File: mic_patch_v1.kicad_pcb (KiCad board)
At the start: 4 copper layers, 40 x 31 mm, 56 parts, among them J1 Conn_ARM_SWD_TagConnect_TC203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, J2 J_000002, J3 J_000001, J4 Micro_SD_Card, J5 J_000003, SW1 SW_000001, SW2 SW_000001, U1 NORA-B106-00B, U2 PWR_nPM1100-QDXX, U3 ADAU7002ACBZ-R7, Y1 CLK_0003

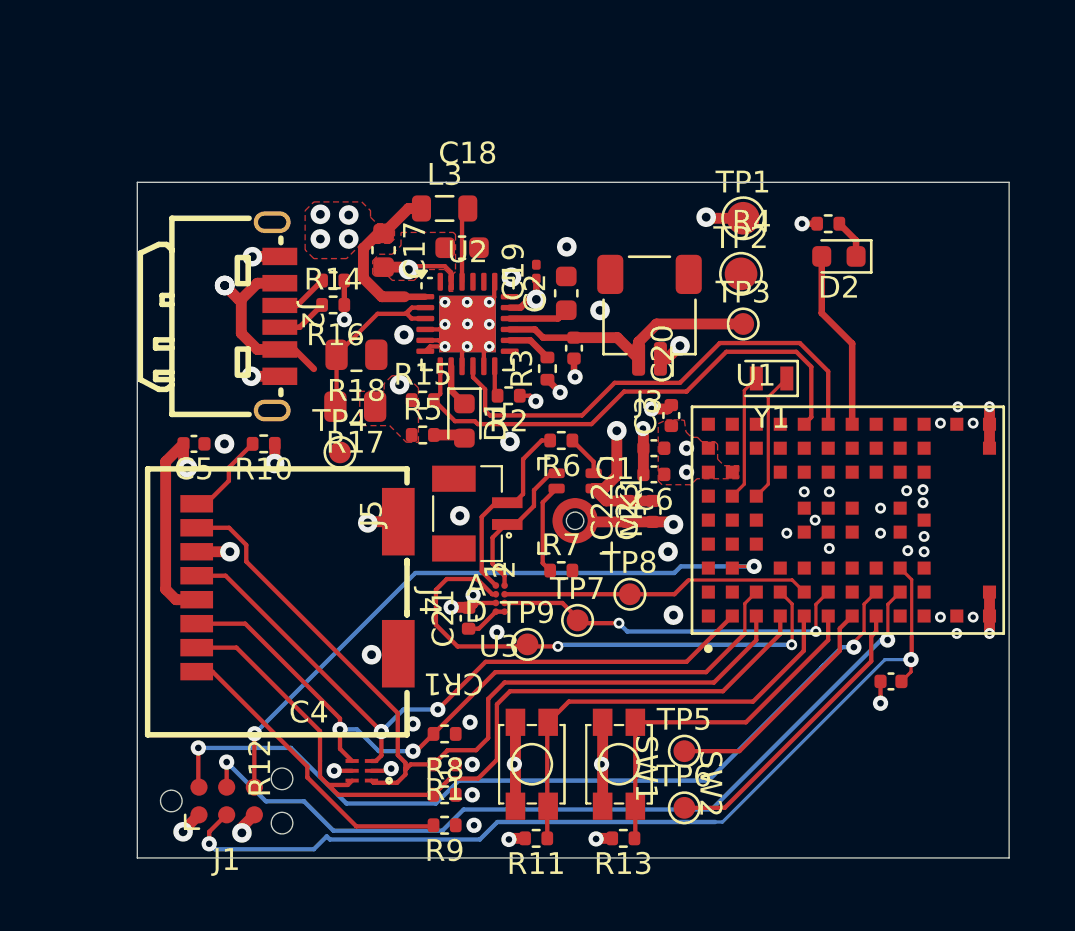
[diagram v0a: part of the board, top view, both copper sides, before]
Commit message: poured additional ground planes
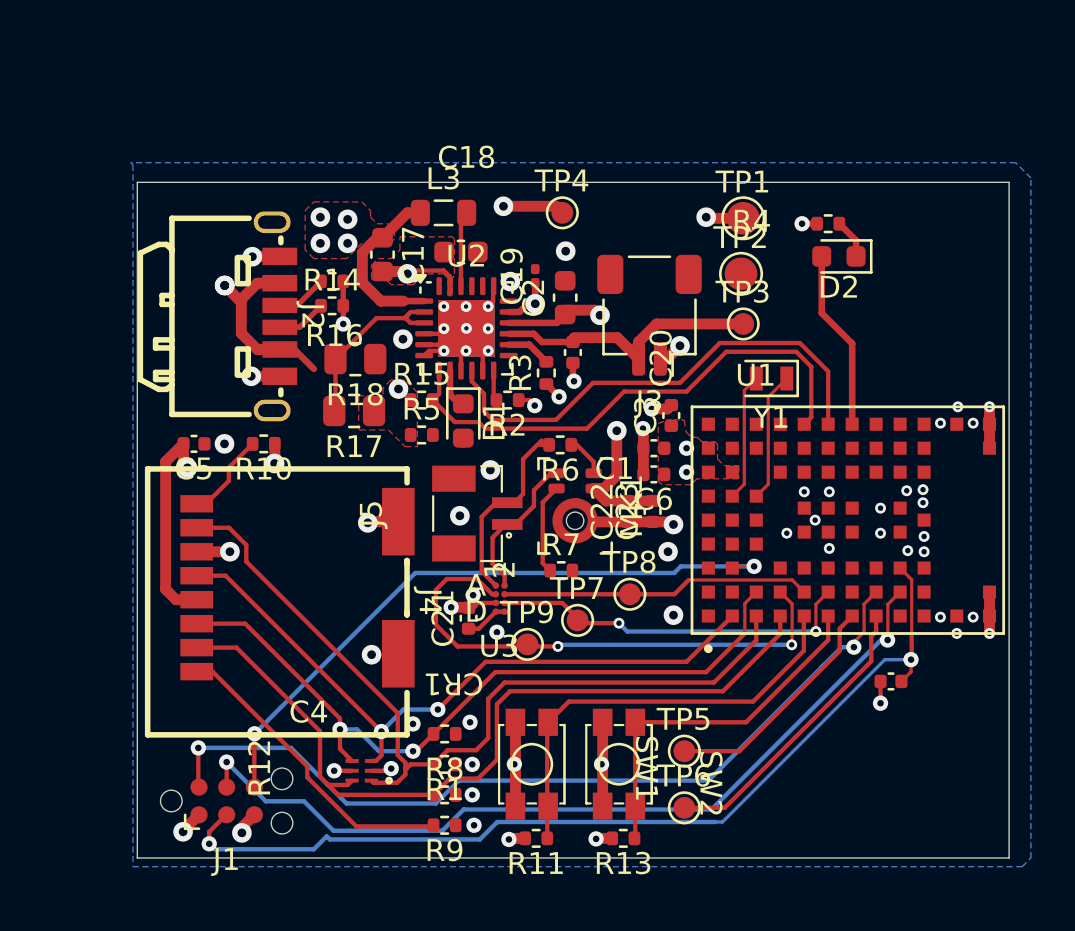
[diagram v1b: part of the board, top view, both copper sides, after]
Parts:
- moved TP4 15.0 mm to (149.4, 90.9)
- moved C18 0.21 mm to (144.8, 92.7)
- moved C19 0.21 mm to (148.2, 93.8)
- moved L3 0.21 mm to (143.9, 90.9)
- moved R17 0.21 mm to (139.8, 100.0)
- moved R3 0.21 mm to (148.7, 98.2)
- moved R6 0.21 mm to (149.3, 101.5)
- moved U2 0.21 mm to (145.0, 96.2)
- moved R2 0.21 mm to (146.9, 99.5)
- moved C2 0.21 mm to (149.5, 94.8)
- moved C20 0.21 mm to (149.9, 97.3)
- moved R18 0.21 mm to (139.9, 97.6)
- moved C17 0.21 mm to (141.2, 92.8)
- moved R16 0.06 mm to (138.8, 94.0)
- moved R14 0.06 mm to (138.8, 95.2)
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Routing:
- net +3V0 VDD_NRF: track 152.2 -> 189.1 mm
- net GND: track 49.0 -> 40.5 mm
- net /Power/VBUS: track 30.6 -> 34.8 mm, vias 3 -> 4
- net VSYS: track 13.6 -> 15.6 mm
- net Net-(D1-A): track 1.46 -> 0.21 mm
- added copper zone on In2.Cu, net +3V0 VDD_NRF
- added copper zone on B.Cu, net GND
- added copper zone on In2.Cu, net GND

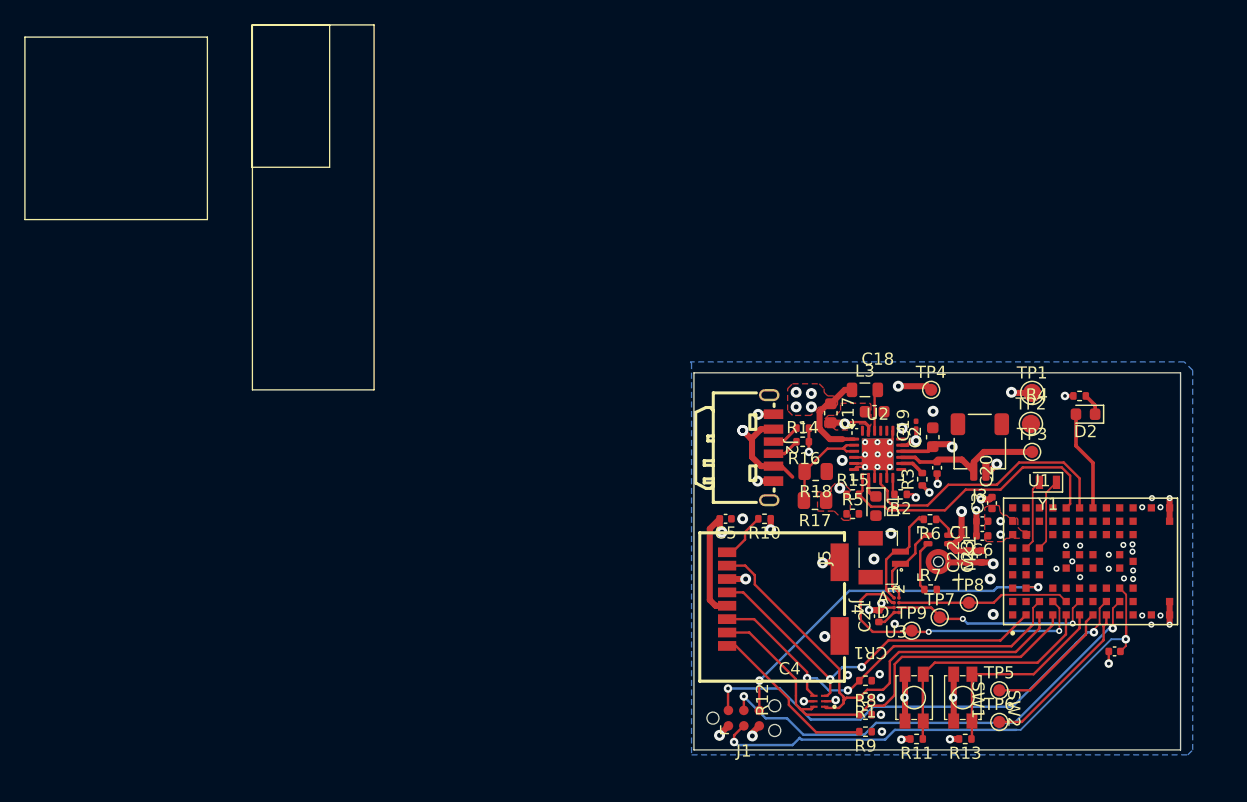
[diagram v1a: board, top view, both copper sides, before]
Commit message: fixed all major DRC warnings and errors
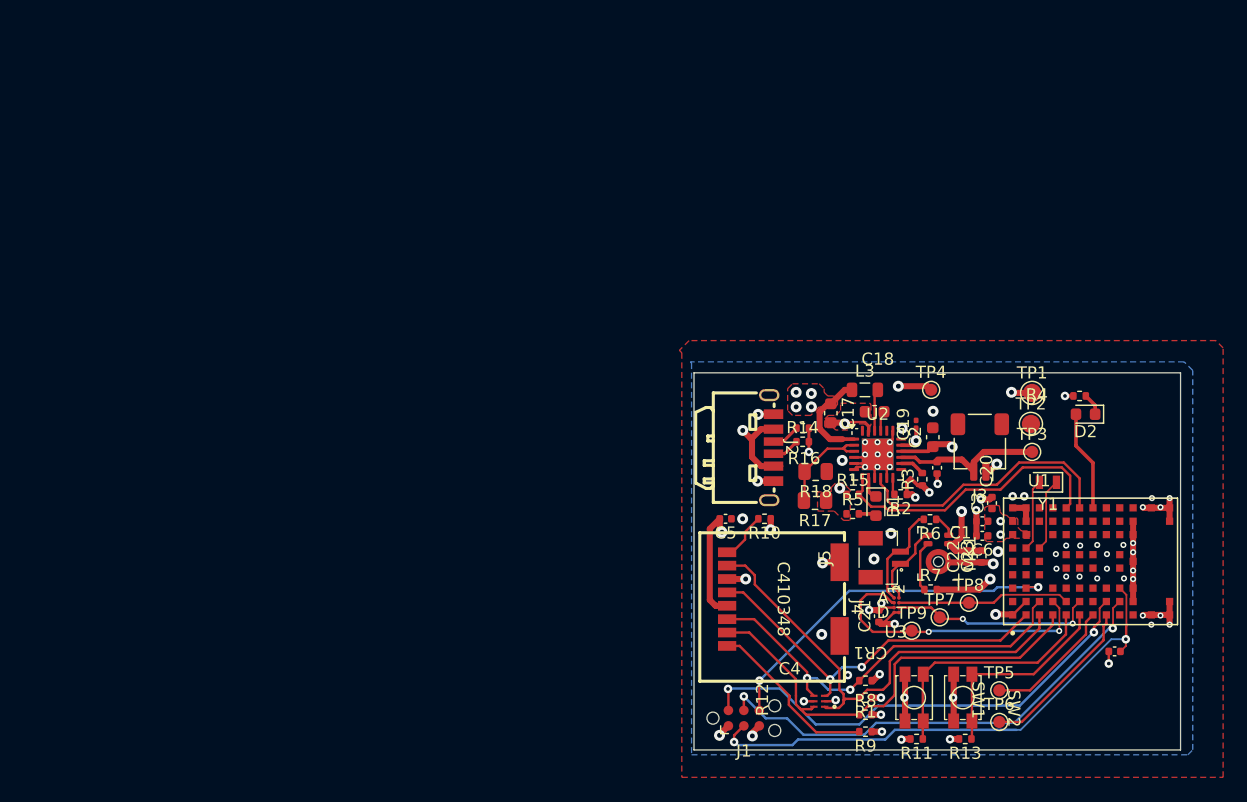
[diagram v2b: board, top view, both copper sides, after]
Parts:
- moved C19 0.07 mm to (148.2, 93.7)
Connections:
- J4 pad 10: (no net) -> GND
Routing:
- net GND: track 40.5 -> 64.1 mm, vias 62 -> 68
- net +3V0 VDD_NRF: track 189.1 -> 194.9 mm
- net /Power/DEC_NPM: track 0.00 -> 1.68 mm
- net Net-(D1-A): track 0.21 -> 1.66 mm
- net /Power/VBUS: track 34.8 -> 33.8 mm, vias 4 -> 3

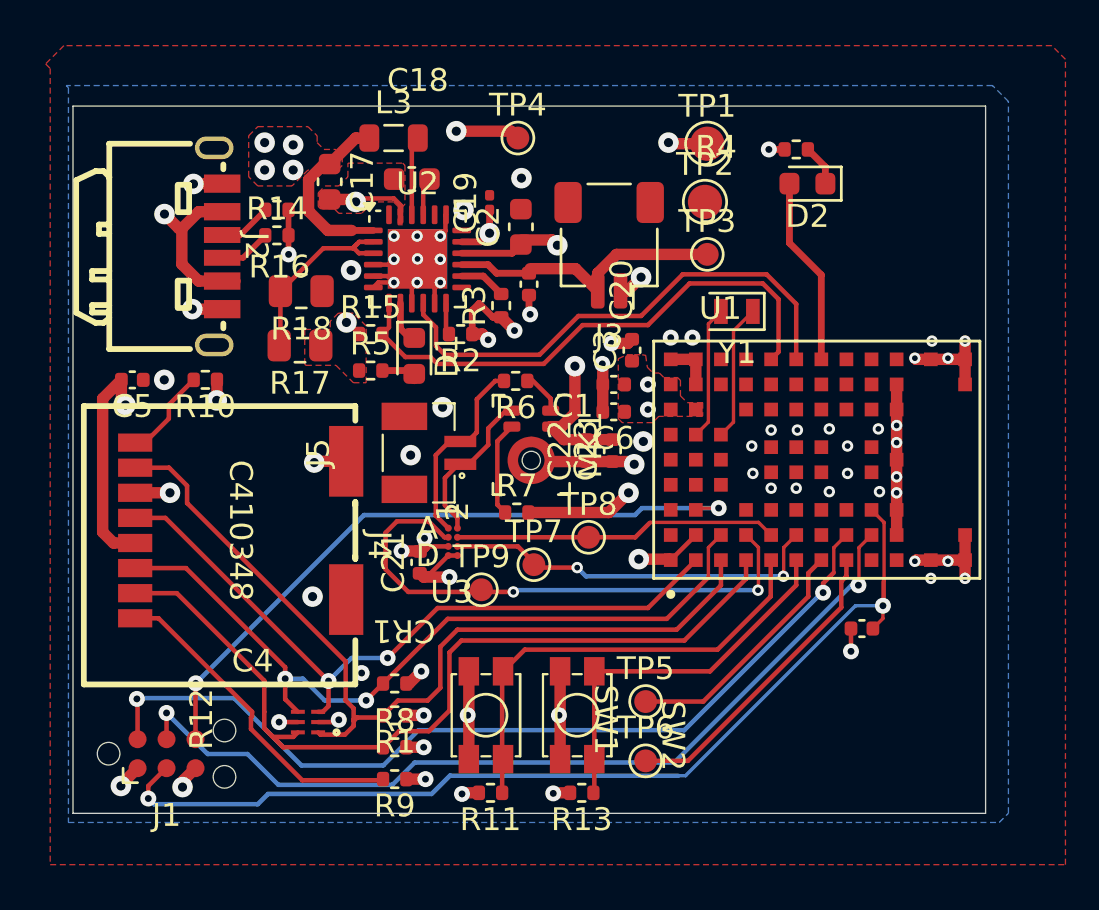
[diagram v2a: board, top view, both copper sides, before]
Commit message: added silkscreen
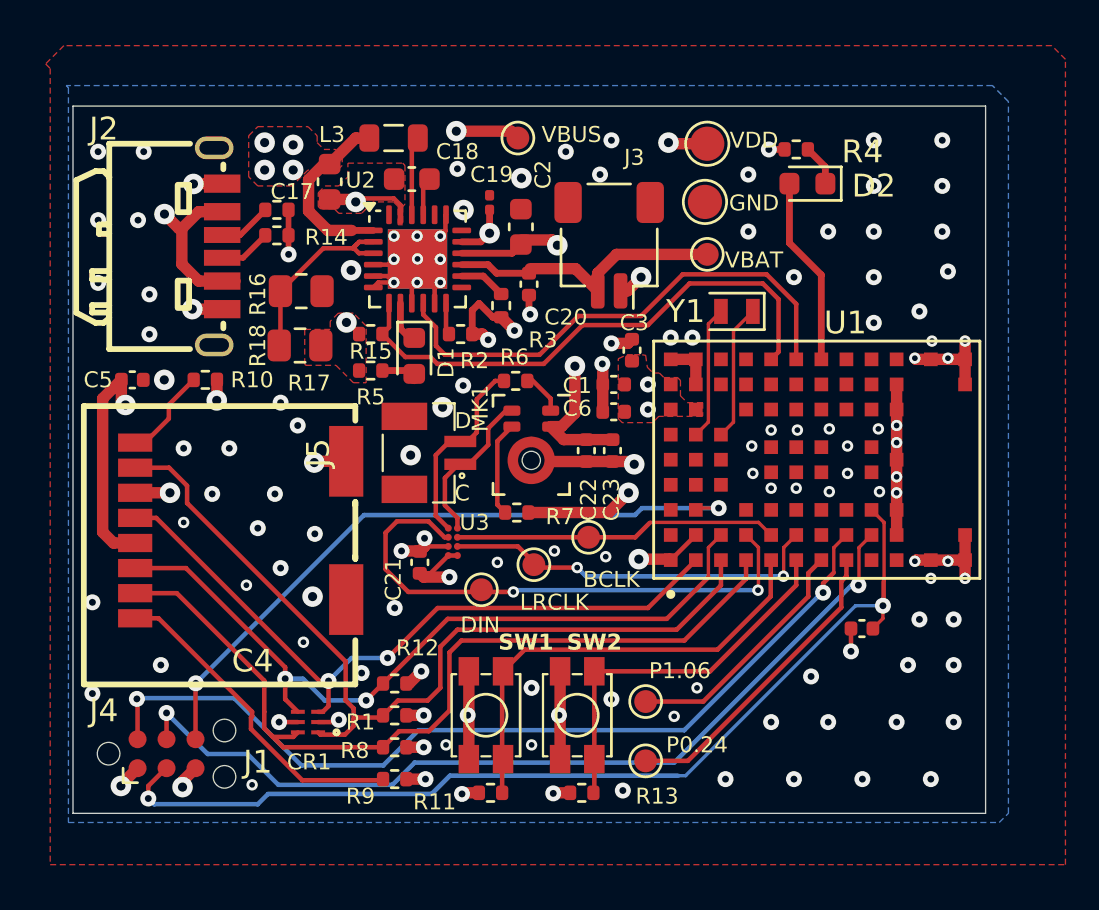
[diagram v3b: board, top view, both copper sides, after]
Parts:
- renumbered TP8 to BCLK, TP9 to DIN, TP2 to GND, TP7 to LRCLK, TP6 to P0.24, TP5 to P1.06, TP3 to VBAT, TP4 to VBUS, TP1 to VDD
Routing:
- net GND: vias 68 -> 133
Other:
- board text added: "C"
- board text added: "D"

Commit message: removed PDM series termination resistor under guidance from MS-2472 analogue devices
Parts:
- removed R6: R_00005, Resistor_SMD:R_0402_1005Metric
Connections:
- MK1 pad 1: Net-(MK1-DATA) -> /Mic/PDM_DAT
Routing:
- net Net-(MK1-DATA): track 1.91 -> 0.00 mm
- net /Mic/PDM_DAT: track 8.62 -> 10.5 mm

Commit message: final tweaks
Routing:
- net GND: vias 133 -> 134
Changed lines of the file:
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@@
 	)
 	(via
-		(at 139 102.5)
+		(at 138.75 102.25)
 		(size 0.7)
 		(drill 0.3)
@@
 		(size 0.7)
 		(drill 0.3)
+		(layers "F.Cu" "B.Cu")
+		(free yes)
+		(net 1)
+	)
+	(via
+		(at 151.5 99.75)
+		(size 0.5)
+		(drill 0.25)
 		(layers "F.Cu" "B.Cu")
 		(free yes)
@@
 	)
 	(segment
+		(start 145.809 99.199)
+		(end 145.809 100.009)
+		(width 0.2)
+		(layer "F.Cu")
+		(net 12)
+	)
+	(segment
+		(start 151.05 98.7)
+		(end 154.8 98.7)
+		(width 0.2)
+		(layer "F.Cu")
+		(net 12)
+	)
+	(segment
 		(start 145.25 98.64)
 		(end 145.809 99.199)
@@
 	)
 	(segment
+		(start 154.8 98.7)
+		(end 156.625 96.875)
+		(width 0.2)
+		(layer "F.Cu")
+		(net 12)
+	)
+	(segment
+		(start 161.6 98.175)
+		(end 161.6 100.6)
+		(width 0.2)
+		(layer "F.Cu")
+		(net 12)
+	)
+	(segment
+		(start 149.35 100.4)
+		(end 151.05 98.7)
+		(width 0.2)
+		(layer "F.Cu")
+		(net 12)
+	)
+	(segment
 		(start 145.809 100.009)
 		(end 146.2 100.4)
@@
 	)
 	(segment
-		(start 161.6 98.175)
-		(end 161.6 100.6)
+		(start 156.625 96.875)
+		(end 160.3 96.875)
 		(width 0.2)
 		(layer "F.Cu")
@@
 	)
 	(segment
-		(start 150.35 100.4)
-		(end 152.05 98.7)
+		(start 146.2 100.4)
+		(end 149.35 100.4)
 		(width 0.2)
 		(layer "F.Cu")
@@
 	)
 	(segment
-		(start 145.809 99.199)
-		(end 145.809 100.009)
-		(width 0.2)
-		(layer "F.Cu")
-		(net 12)
-	)
-	(segment
-		(start 154.8 98.7)
-		(end 156.625 96.875)
+		(start 160.3 96.875)
+		(end 161.6 98.175)
 		(width 0.2)
 		(layer "F.Cu")
@@
 		(start 145.25 98.1375)
 		(end 145.25 98.64)
-		(width 0.2)
-		(layer "F.Cu")
-		(net 12)
-	)
-	(segment
-		(start 156.625 96.875)
-		(end 160.3 96.875)
-		(width 0.2)
-		(layer "F.Cu")
-		(net 12)
-	)
-	(segment
-		(start 146.2 100.4)
-		(end 150.35 100.4)
-		(width 0.2)
-		(layer "F.Cu")
-		(net 12)
-	)
-	(segment
-		(start 160.3 96.875)
-		(end 161.6 98.175)
-		(width 0.2)
-		(layer "F.Cu")
-		(net 12)
-	)
-	(segment
-		(start 152.05 98.7)
-		(end 154.8 98.7)
 		(width 0.2)
 		(layer "F.Cu")
@@
 	)
 	(segment
+		(start 156.925 97.275)
+		(end 160.134314 97.275)
+		(width 0.2)
+		(layer "F.Cu")
+		(net 27)
+	)
+	(segment
+		(start 143.75 98.1375)
+		(end 143.75 99.202)
+		(width 0.2)
+		(layer "F.Cu")
+		(net 27)
+	)
+	(segment
+		(start 143.75 99.202)
+		(end 143.46 99.492)
+		(width 0.2)
+		(layer "F.Cu")
+		(net 27)
+	)
+	(segment
+		(start 160.825 97.965686)
+		(end 160.825 100.275)
+		(width 0.2)
+		(layer "F.Cu")
+		(net 27)
+	)
+	(segment
 		(start 160.825 100.275)
 		(end 160.5 100.6)
@@
 	)
 	(segment
-		(start 160.825 97.965686)
-		(end 160.825 100.275)
+		(start 145.867314 100.8)
+		(end 149.515686 100.8)
+		(width 0.2)
+		(layer "F.Cu")
+		(net 27)
+	)
+	(segment
+		(start 155.1 99.1)
+		(end 156.925 97.275)
+		(width 0.2)
+		(layer "F.Cu")
+		(net 27)
+	)
+	(segment
+		(start 149.515686 100.8)
+		(end 151.215686 99.1)
+		(width 0.2)
+		(layer "F.Cu")
+		(net 27)
+	)
+	(segment
+		(start 143.46 99.492)
+		(end 144.468 100.5)
+		(width 0.2)
+		(layer "F.Cu")
+		(net 27)
+	)
+	(segment
+		(start 145.567314 100.5)
+		(end 145.867314 100.8)
 		(width 0.2)
 		(layer "F.Cu")
@@
 	)
 	(segment
-		(start 143.75 98.1375)
-		(end 143.75 99.202)
-		(width 0.2)
-		(layer "F.Cu")
-		(net 27)
-	)
-	(segment
-		(start 143.75 99.202)
-		(end 143.46 99.492)
-		(width 0.2)
-		(layer "F.Cu")
-		(net 27)
-	)
-	(segment
-		(start 145.867314 100.8)
-		(end 150.533 100.8)
-		(width 0.2)
-		(layer "F.Cu")
-		(net 27)
-	)
-	(segment
 		(start 160.134314 97.275)
 		(end 160.825 97.965686)
@@
 	)
 	(segment
-		(start 156.925 97.275)
-		(end 160.134314 97.275)
-		(width 0.2)
-		(layer "F.Cu")
-		(net 27)
-	)
-	(segment
-		(start 143.46 99.492)
-		(end 144.468 100.5)
-		(width 0.2)
-		(layer "F.Cu")
-		(net 27)
-	)
-	(segment
-		(start 145.567314 100.5)
-		(end 145.867314 100.8)
-		(width 0.2)
-		(layer "F.Cu")
-		(net 27)
-	)
-	(segment
-		(start 152.233 99.1)
+		(start 151.215686 99.1)
 		(end 155.1 99.1)
 		(width 0.2)
 		(layer "F.Cu")
-		(net 27)
-	)
-	(segment
-		(start 150.533 100.8)
-		(end 152.233 99.1)
-		(width 0.2)
-		(layer "F.Cu")
-		(net 27)
-	)
-	(segment
-		(start 155.1 99.1)
-		(end 156.925 97.275)
-		(width 0.2)
-		(layer "F.Cu")
